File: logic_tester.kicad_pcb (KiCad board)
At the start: 2 copper layers, 66 x 12 mm, 37 parts, among them J1 15EDGR-3.5-02P, J2 Probe, U1 LM339D, U2 LM317MDT

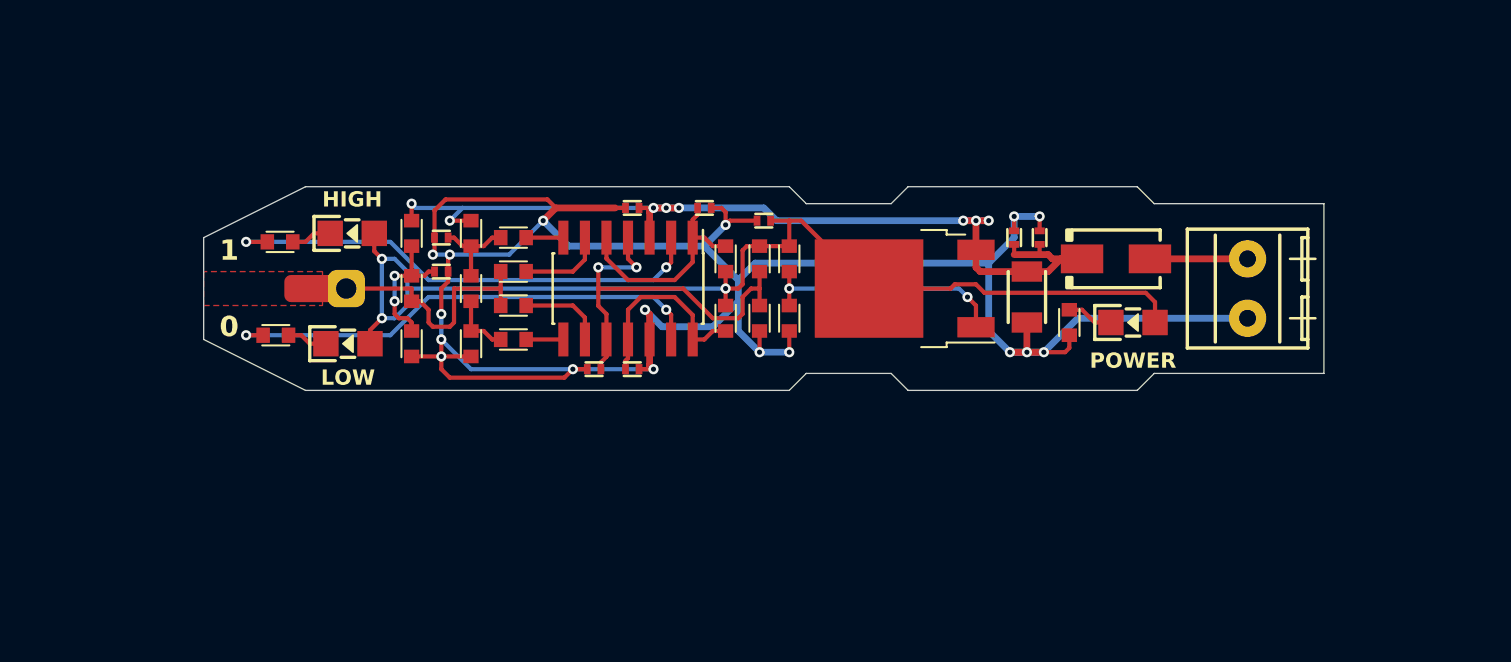
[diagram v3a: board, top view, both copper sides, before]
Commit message: Ground plane + more silk
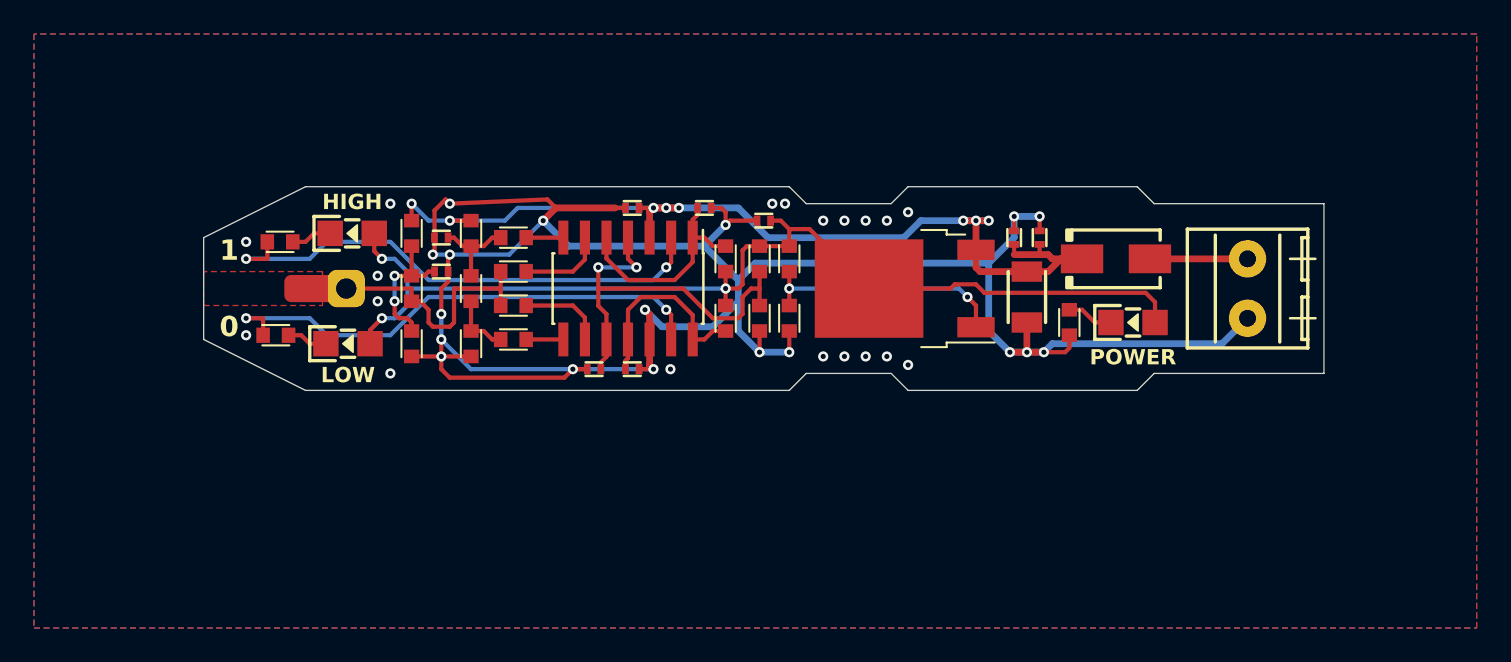
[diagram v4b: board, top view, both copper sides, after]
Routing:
- net /VCC_REG: track 66.9 -> 62.9 mm
- net Net-(R17-Pad1): track 29.1 -> 30.5 mm
- net Net-(R19-Pad1): track 28.9 -> 30.3 mm
- net GNDD: track 142.4 -> 142.5 mm, vias 17 -> 37
- added copper zone on B.Cu, net GNDD
- added copper zone on F.Cu, net GNDD
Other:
- board text added: "+12V"
- board text added: "GND"
- board text added: "LOG 0"
- board text added: "LOG 1"
- board text added: "PROBE"

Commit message: Title added to sheets
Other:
- board text added: "+"
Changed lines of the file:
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@@
   )
   (paper "A4")
+  (title_block
+    (title "Logic Tester")
+    (date "2024-11-23")
+    (rev "1.0")
+    (company "OSHW")
+  )
   (layers
     (0 "F.Cu" signal)
@@
     (effects (font (size 0.9 0.9) (thickness 0.2) bold))
   )
+  (gr_text "+" (at 129.5 95.25) (layer "F.SilkS")
+    (effects (font (size 1.5 1.5) (thickness 0.3) bold))
+  )
   (segment (start 104.1 95.65) (end 104.1 95.25) (width 0.25) (layer "F.Cu") (net 1))

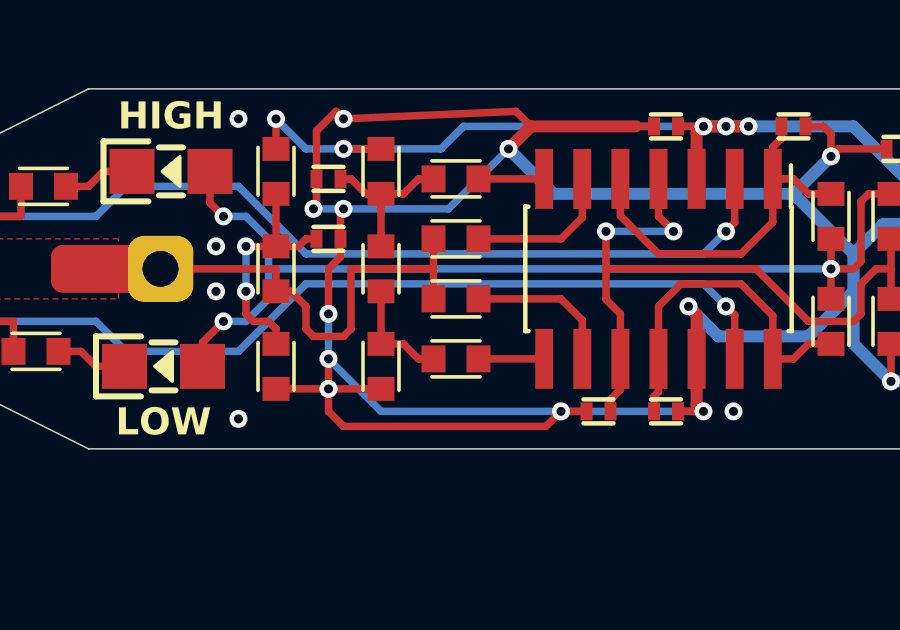
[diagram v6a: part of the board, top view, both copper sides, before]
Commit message: QR code added (generated by nayuki.io)
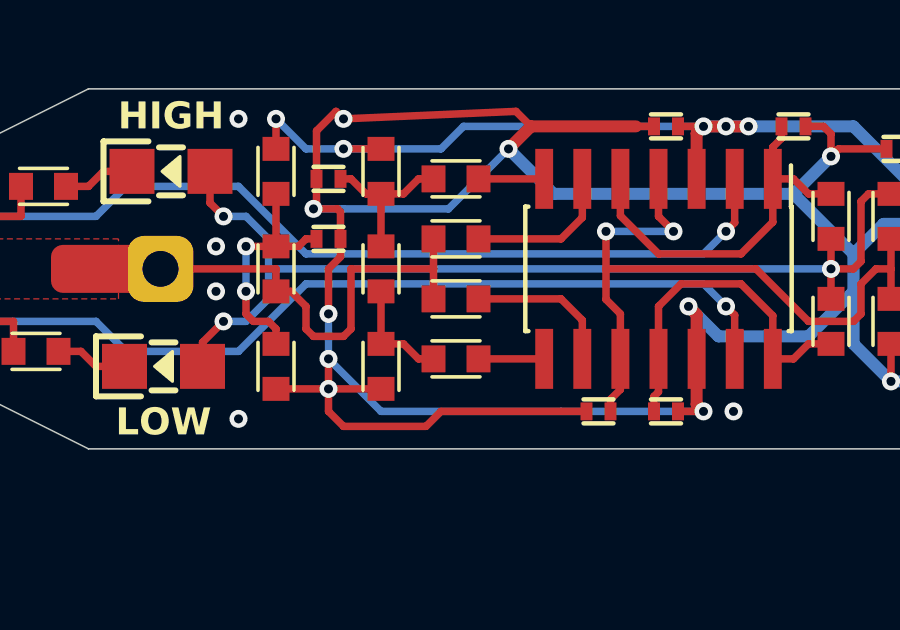
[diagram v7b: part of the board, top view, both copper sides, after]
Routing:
- net GNDD: track 142.5 -> 143.3 mm, vias 37 -> 35
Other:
- board text added: "+5..24V"
- board text added: "-"
- board text added: "Open Logic Tester"
- board text added: "github.com/Nevada317/logic_tester"
- board text removed: "+12V"
